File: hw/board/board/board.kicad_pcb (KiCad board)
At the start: 2 copper layers, 36 parts, among them J1 DB15_Female_HighDensity_Mount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, J2 10029449-111RLF, J3 SI-50170-F, J4 USB4085-GF-A_REVB, J5 USB_A_Stacked, J6 USB_A_Stacked, SW1 SW_DIP_x08, SW2 SW_Push, SW3 SW_Push, U18 MAX3421E, U19 TUSB2046BVFR, U20 FT4232H, U7 W65C02P

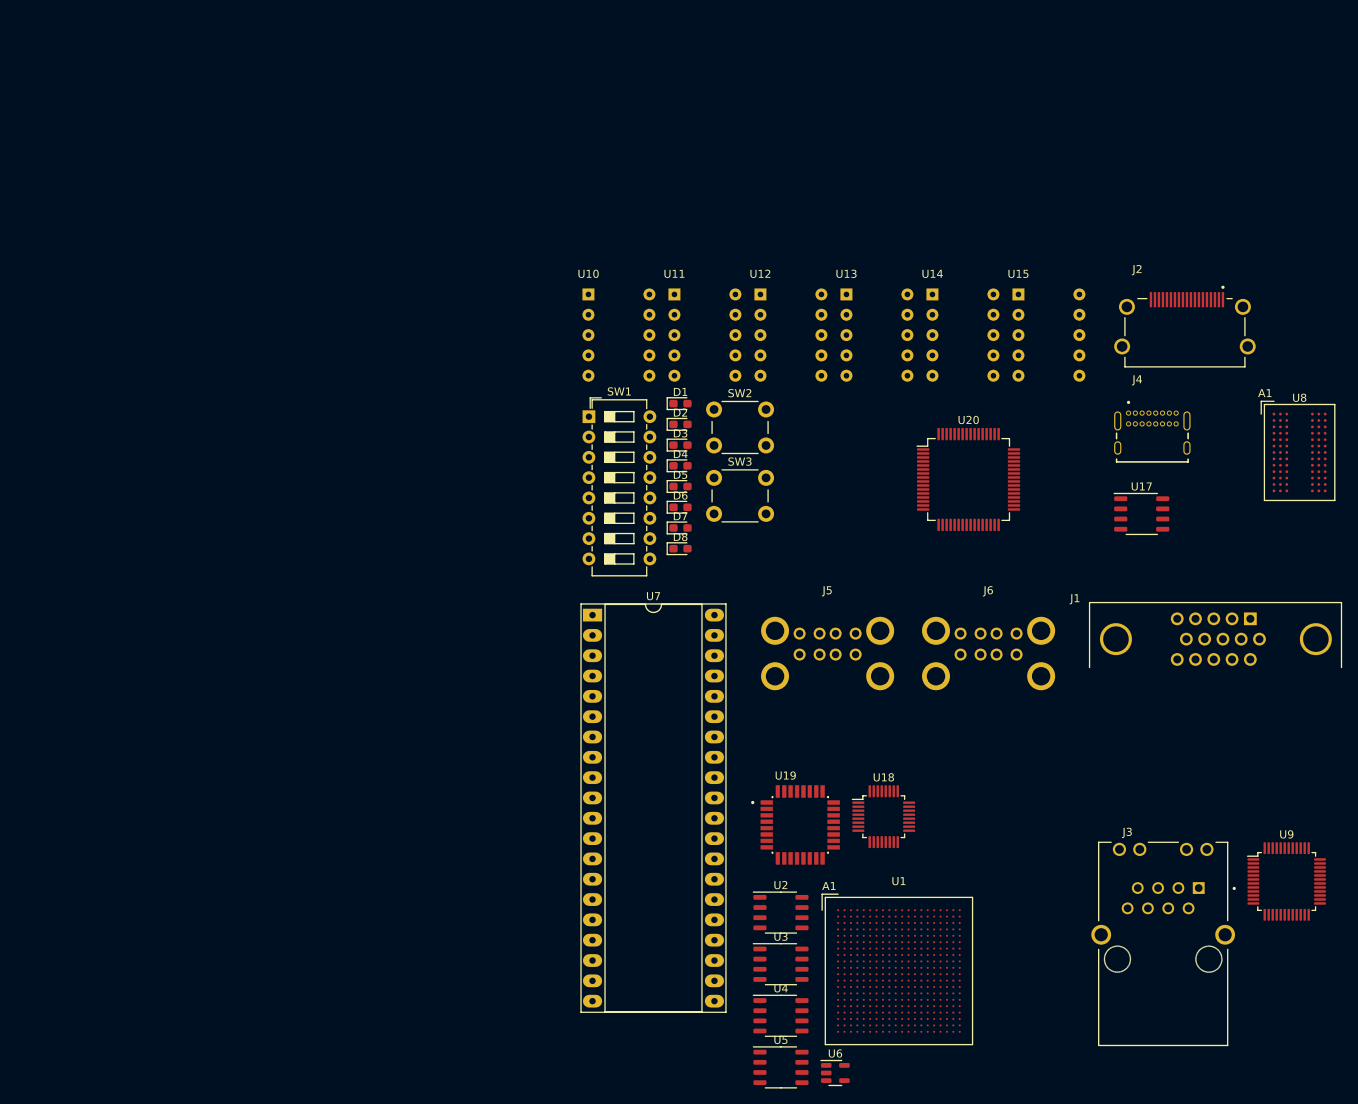
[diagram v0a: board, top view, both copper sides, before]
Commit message: Add wires to fpga block (but don't connect them)
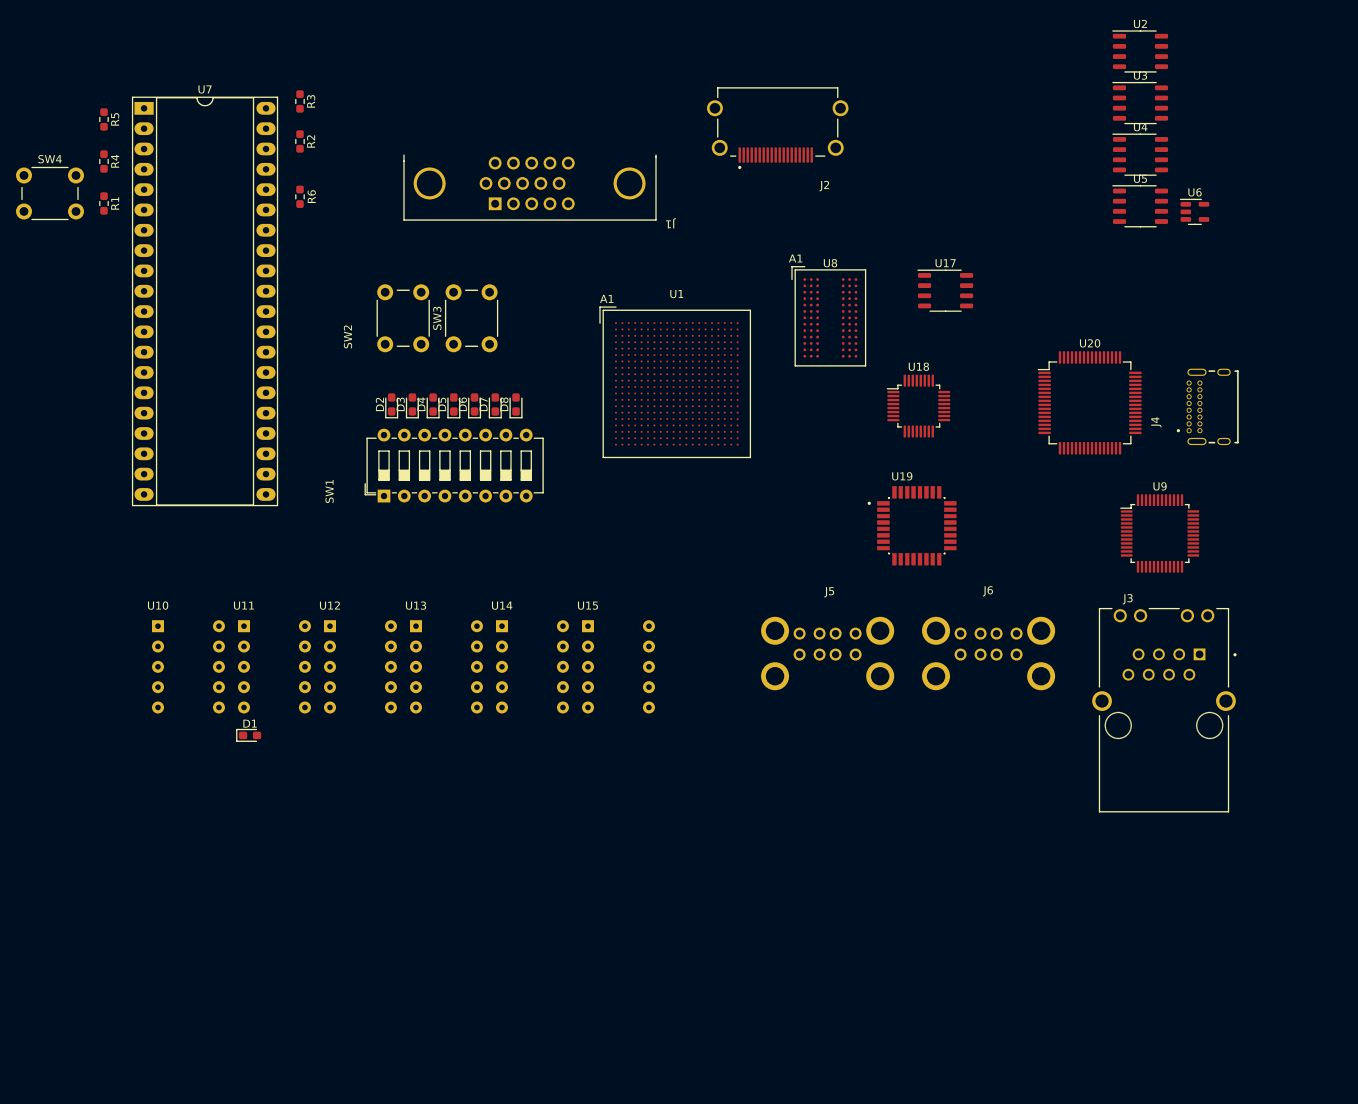
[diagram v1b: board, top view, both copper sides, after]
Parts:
- added R1: 10K, Resistor_SMD:R_0603_1608Metric_Pad0.98x0.95mm_HandSolder, F.Cu at (34.0, 37.5)
- added R2: 10K, Resistor_SMD:R_0603_1608Metric_Pad0.98x0.95mm_HandSolder, F.Cu at (58.5, 29.8)
- added R3: 10K, Resistor_SMD:R_0603_1608Metric_Pad0.98x0.95mm_HandSolder, F.Cu at (58.5, 24.8)
- added R4: 10K, Resistor_SMD:R_0603_1608Metric_Pad0.98x0.95mm_HandSolder, F.Cu at (34.0, 32.2)
- added R5: 10K, Resistor_SMD:R_0603_1608Metric_Pad0.98x0.95mm_HandSolder, F.Cu at (34.0, 27.0)
- added R6: 10K, Resistor_SMD:R_0603_1608Metric_Pad0.98x0.95mm_HandSolder, F.Cu at (58.5, 36.7)
- added SW4: SW_Push, Button_Switch_THT:SW_PUSH_6mm_H5mm, F.Cu at (24.0, 34.0)
- moved U5 116.6 mm to (163.6, 37.9)
- moved U2 116.6 mm to (163.6, 18.5)
- moved U3 116.6 mm to (163.6, 24.9)
- moved U6 116.6 mm to (170.4, 38.5)
- moved U4 116.6 mm to (163.6, 31.4)
- moved U7 84.6 mm to (39.0, 25.6)
- moved J1 83.3 mm to (99.7, 35.0), turned to 180 degrees
- moved U1 78.5 mm to (105.6, 60.0)
- moved U10 67.9 mm to (40.8, 90.3)
- moved U11 67.9 mm to (51.5, 90.3)
- moved U12 67.9 mm to (62.2, 90.3)
- moved U13 67.9 mm to (73.0, 90.3)
- moved U14 67.9 mm to (83.8, 90.3)
- moved U15 67.9 mm to (94.5, 90.3)
- moved D1 67.9 mm to (52.3, 104.0)
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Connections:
- U7 pad 1: unconnected-(U7-~{VPB}-Pad1) -> /cpu/~{CPU_VPB}
- U7 pad 10: unconnected-(U7-A1-Pad10) -> /cpu/CPU_ADDR1
- U7 pad 11: unconnected-(U7-A2-Pad11) -> /cpu/CPU_ADDR2
- U7 pad 12: unconnected-(U7-A3-Pad12) -> /cpu/CPU_ADDR3
- U7 pad 13: unconnected-(U7-A4-Pad13) -> /cpu/CPU_ADDR4
- U7 pad 14: unconnected-(U7-A5-Pad14) -> /cpu/CPU_ADDR5
- U7 pad 15: unconnected-(U7-A6-Pad15) -> /cpu/CPU_ADDR6
- U7 pad 16: unconnected-(U7-A7-Pad16) -> /cpu/CPU_ADDR7
- U7 pad 17: unconnected-(U7-A8-Pad17) -> /cpu/CPU_ADDR8
- U7 pad 18: unconnected-(U7-A9-Pad18) -> /cpu/CPU_ADDR9
- U7 pad 19: unconnected-(U7-A10-Pad19) -> /cpu/CPU_ADDR10
- U7 pad 2: unconnected-(U7-RDY-Pad2) -> /cpu/CPU_RDY
- U7 pad 20: unconnected-(U7-A11-Pad20) -> /cpu/CPU_ADDR11
- U7 pad 21: unconnected-(U7-VSS-Pad21) -> GND
- U7 pad 22: unconnected-(U7-A12-Pad22) -> /cpu/CPU_ADDR12
- U7 pad 23: unconnected-(U7-A13-Pad23) -> /cpu/CPU_ADDR13
- U7 pad 24: unconnected-(U7-A14-Pad24) -> /cpu/CPU_ADDR14
- U7 pad 25: unconnected-(U7-A15-Pad25) -> /cpu/CPU_ADDR15
- U7 pad 26: unconnected-(U7-D7-Pad26) -> /cpu/CPU_DATA7
- U7 pad 27: unconnected-(U7-D6-Pad27) -> /cpu/CPU_DATA6
- U7 pad 28: unconnected-(U7-D5-Pad28) -> /cpu/CPU_DATA5
- U7 pad 29: unconnected-(U7-D4-Pad29) -> /cpu/CPU_DATA4
- U7 pad 30: unconnected-(U7-D3-Pad30) -> /cpu/CPU_DATA3
- U7 pad 31: unconnected-(U7-D2-Pad31) -> /cpu/CPU_DATA2
- U7 pad 32: unconnected-(U7-D1-Pad32) -> /cpu/CPU_DATA1
- U7 pad 33: unconnected-(U7-D0-Pad33) -> /cpu/CPU_DATA0
- U7 pad 34: unconnected-(U7-~{RWB}-Pad34) -> /cpu/~{CPU_RWB}
- U7 pad 36: unconnected-(U7-BE-Pad36) -> /cpu/CPU_BE
- U7 pad 37: unconnected-(U7-PHI2-Pad37) -> /cpu/CPU_PHI2
- U7 pad 38: unconnected-(U7-~{SOB}-Pad38) -> Net-(U7-~{SOB})
- U7 pad 4: unconnected-(U7-~{IRQB}-Pad4) -> /cpu/~{CPU_IRQB}
- U7 pad 40: unconnected-(U7-~{RESB}-Pad40) -> /cpu/~{CPU_RESB}
- U7 pad 5: unconnected-(U7-~{MLB}-Pad5) -> /cpu/~{CPU_MLB}
- U7 pad 6: unconnected-(U7-~{NMIB}-Pad6) -> /cpu/~{CPU_NMIB}
- U7 pad 7: unconnected-(U7-SYNC-Pad7) -> /cpu/CPU_SYNC
- U7 pad 8: unconnected-(U7-VDD-Pad8) -> +3V3
- U7 pad 9: unconnected-(U7-A0-Pad9) -> /cpu/CPU_ADDR0

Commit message: Start work on ddr
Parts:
- added R10: 15R, Resistor_SMD:R_0402_1005Metric, F.Cu at (218.2, 77.5)
- added R11: 15R, Resistor_SMD:R_0402_1005Metric, F.Cu at (225.2, 77.5)
- added R12: 15R, Resistor_SMD:R_0402_1005Metric, F.Cu at (221.2, 77.5)
- added R13: 15R, Resistor_SMD:R_0402_1005Metric, F.Cu at (223.2, 77.5)
- added R14: 15R, Resistor_SMD:R_0402_1005Metric, F.Cu at (220.2, 77.5)
- added R15: 15R, Resistor_SMD:R_0402_1005Metric, F.Cu at (222.2, 77.5)
- added R17: 15R, Resistor_SMD:R_0402_1005Metric, F.Cu at (225.2, 44.6)
- added R18: 15R, Resistor_SMD:R_0402_1005Metric, F.Cu at (225.2, 47.1)
- added R19: 240R, Resistor_SMD:R_0402_1005Metric, F.Cu at (225.2, 49.6)
- added R20: 1k, Resistor_SMD:R_0402_1005Metric, F.Cu at (225.2, 52.1)
- added R21: 1k, Resistor_SMD:R_0402_1005Metric, F.Cu at (225.2, 54.6)
- added R22: 40R, Resistor_SMD:R_0402_1005Metric, F.Cu at (220.6, 94.3)
- added R23: 40R, Resistor_SMD:R_0402_1005Metric, F.Cu at (223.6, 94.3)
- added R24: 40R, Resistor_SMD:R_0402_1005Metric, F.Cu at (217.6, 94.3)
- added R25: 40R, Resistor_SMD:R_0402_1005Metric, F.Cu at (214.6, 88.0)
- added R26: 40R, Resistor_SMD:R_0402_1005Metric, F.Cu at (229.0, 89.0)
- added R27: 40R, Resistor_SMD:R_0402_1005Metric, F.Cu at (214.6, 89.0)
- added R28: 40R, Resistor_SMD:R_0402_1005Metric, F.Cu at (229.0, 90.0)
- added R29: 40R, Resistor_SMD:R_0402_1005Metric, F.Cu at (214.6, 90.0)
- added R30: 40R, Resistor_SMD:R_0402_1005Metric, F.Cu at (229.0, 91.0)
- added R31: 40R, Resistor_SMD:R_0402_1005Metric, F.Cu at (219.6, 94.3)
- added R32: 40R, Resistor_SMD:R_0402_1005Metric, F.Cu at (229.0, 87.0)
- added R33: 40R, Resistor_SMD:R_0402_1005Metric, F.Cu at (224.6, 94.3)
- added R34: 40R, Resistor_SMD:R_0402_1005Metric, F.Cu at (222.6, 94.3)
- added R35: 40R, Resistor_SMD:R_0402_1005Metric, F.Cu at (218.6, 94.3)
- added R36: 40R, Resistor_SMD:R_0402_1005Metric, F.Cu at (225.6, 94.3)
- added R37: 40R, Resistor_SMD:R_0402_1005Metric, F.Cu at (214.6, 87.0)
- added R38: 40R, Resistor_SMD:R_0402_1005Metric, F.Cu at (229.0, 88.0)
- added R39: 40R, Resistor_SMD:R_0402_1005Metric, F.Cu at (221.6, 94.3)
- added R40: 40R, Resistor_SMD:R_0402_1005Metric, F.Cu at (233.9, 52.1)
- added R41: 40R, Resistor_SMD:R_0402_1005Metric, F.Cu at (233.9, 54.6)
- added R42: 40R, Resistor_SMD:R_0402_1005Metric, F.Cu at (233.9, 57.1)
- added R43: 40R, Resistor_SMD:R_0402_1005Metric, F.Cu at (233.9, 59.7)
- added R44: 40R, Resistor_SMD:R_0402_1005Metric, F.Cu at (233.9, 62.2)
- added R45: 40R, Resistor_SMD:R_0402_1005Metric, F.Cu at (233.9, 64.7)
- added R46: 240R, Resistor_SMD:R_0402_1005Metric, F.Cu at (240.3, 44.6)
- added R7: 100R, Resistor_SMD:R_0402_1005Metric, F.Cu at (220.9, 44.6)
- added R8: 15R, Resistor_SMD:R_0402_1005Metric, F.Cu at (219.2, 77.5)
- added R9: 15R, Resistor_SMD:R_0402_1005Metric, F.Cu at (224.2, 77.5)
- moved U1 152.7 mm to (256.2, 85.2)
- moved U8 102.7 mm to (221.8, 85.4)
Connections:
- U1 pad K1: unconnected-(U1K-DDR_BA2-PadK1) -> /ddr/DDR_BA2
- U1 pad K2: unconnected-(U1K-DDR_BA2-PadK2) -> /ddr/DDR_BA1
- U1 pad K3: unconnected-(U1K-DDR_BA0-PadK3) -> /ddr/DDR_BA0
- U1 pad K4: unconnected-(U1K-DDR_WE_N-PadK4) -> /ddr/DDR_WE#
- U1 pad L4: unconnected-(U1K-DDR_RST_N-PadL4) -> /ddr/DDR_RESET#
- U1 pad L6: unconnected-(U1K-DDR_ODT-PadL6) -> /ddr/DDR_ODT
- U1 pad L7: unconnected-(U1K-VCCIO_DDR-PadL7) -> +1V35
- U1 pad M4: unconnected-(U1K-DDR_RAS_N-PadM4) -> /ddr/DDR_RAS#
- U1 pad M6: unconnected-(U1K-DDR_A13-PadM6) -> /ddr/DDR_A13
- U1 pad N4: unconnected-(U1K-DDR_A14-PadN4) -> /ddr/DDR_A14
- U1 pad N5: unconnected-(U1K-DDR_A11-PadN5) -> /ddr/DDR_A11
- U1 pad N6: unconnected-(U1K-DDR_CKE-PadN6) -> /ddr/DDR_CKE
- U1 pad N7: unconnected-(U1K-VCCIO_DDR-PadN7) -> +1V35
- U1 pad P4: unconnected-(U1K-DDR_A12-PadP4) -> /ddr/DDR_A12
- U1 pad P5: unconnected-(U1K-VCCIO_DDR-PadP5) -> +1V35
- U1 pad P6: unconnected-(U1K-DDR_CAS_N-PadP6) -> /ddr/DDR_CAS#
- U1 pad R1: unconnected-(U1K-DDR_A8-PadR1) -> /ddr/DDR_A8
- U1 pad R2: unconnected-(U1K-VCCIO_DDR-PadR2) -> +1V35
- U1 pad R3: unconnected-(U1K-DDR_CK-PadR3) -> /ddr/DDR_CK
- U1 pad R4: unconnected-(U1K-DDR_CK_N-PadR4) -> /ddr/DDR_CK#
- U1 pad R5: unconnected-(U1K-DDR_A10-PadR5) -> /ddr/DDR_A10
- U1 pad R6: unconnected-(U1K-DDR_CS_N-PadR6) -> /ddr/DDR_CS#
- U1 pad R7: unconnected-(U1K-VCCIO_DDR-PadR7) -> +1V35
- U1 pad T1: unconnected-(U1K-DDR_A7-PadT1) -> /ddr/DDR_A7
- U1 pad T2: unconnected-(U1K-DDR_A9-PadT2) -> /ddr/DDR_A9
- U1 pad T3: unconnected-(U1K-DDR_A4-PadT3) -> /ddr/DDR_A4
- U1 pad T4: unconnected-(U1K-DDR_A6-PadT4) -> /ddr/DDR_A6
- U1 pad T5: unconnected-(U1K-DDR_A5-PadT5) -> /ddr/DDR_A5
- U1 pad T6: unconnected-(U1K-DDR_A3-PadT6) -> /ddr/DDR_A3
- U1 pad U1: unconnected-(U1K-DDR_DQS_N0-PadU1) -> /ddr/DDR_DQS#
- U1 pad U2: unconnected-(U1K-DDR_DQ3-PadU2) -> /ddr/DDR_DQ3
- U1 pad U3: unconnected-(U1K-DDR_DQ0-PadU3) -> /ddr/DDR_DQ0
- U1 pad U4: unconnected-(U1K-DDR_A0-PadU4) -> /ddr/DDR_A0
- U1 pad V1: unconnected-(U1K-DDR_DQS0-PadV1) -> /ddr/DDR_DQS
- U1 pad V3: unconnected-(U1K-DDR_DQ2-PadV3) -> /ddr/DDR_DQ2
- U1 pad V4: unconnected-(U1K-DDR_VREF-PadV4) -> /fpga/VTT
- U1 pad V5: unconnected-(U1K-DDR_A2-PadV5) -> /ddr/DDR_A2
- U1 pad W1: unconnected-(U1K-DDR_DM0-PadW1) -> /ddr/DDR_DM
- U1 pad W2: unconnected-(U1K-DDR_DQ4-PadW2) -> /ddr/DDR_DQ4
- U1 pad W3: unconnected-(U1K-DDR_DQ1-PadW3) -> /ddr/DDR_DQ1
- U1 pad W4: unconnected-(U1K-VCCIO_DDR-PadW4) -> +1V35
- U1 pad W5: unconnected-(U1K-DDR_A1-PadW5) -> /ddr/DDR_A1
- U1 pad Y2: unconnected-(U1K-DDR_DQ7-PadY2) -> /ddr/DDR_DQ7
- U1 pad Y3: unconnected-(U1K-DDR_DQ5-PadY3) -> /ddr/DDR_DQ5
- U1 pad Y4: unconnected-(U1K-DDR_DQ6-PadY4) -> /ddr/DDR_DQ6
- U1 pad Y5: unconnected-(U1K-DDR_ZQ-PadY5) -> Net-(U1K-DDR_ZQ)
- U8 pad A1: unconnected-(U8A-VSS-PadA1) -> GND
- U8 pad A2: unconnected-(U8A-VDD-PadA2) -> +1V35
- U8 pad A8: unconnected-(U8A-VSS-PadA8) -> GND
- U8 pad A9: unconnected-(U8A-VDD-PadA9) -> +1V35
- U8 pad B1: unconnected-(U8A-VSS-PadB1) -> GND
- U8 pad B2: unconnected-(U8A-VSSQ-PadB2) -> GND
- U8 pad B3: unconnected-(U8B-DQ0-PadB3) -> Net-(U8B-DQ0)
- U8 pad B7: unconnected-(U8B-DM/TDQS-PadB7) -> Net-(U8B-DM/TDQS)
- U8 pad B8: unconnected-(U8A-VSSQ-PadB8) -> GND
- U8 pad B9: unconnected-(U8A-VDDQ-PadB9) -> +1V35
- U8 pad C1: unconnected-(U8A-VDDQ-PadC1) -> +1V35
- U8 pad C2: unconnected-(U8B-DQ2-PadC2) -> Net-(U8B-DQ2)
- U8 pad C3: unconnected-(U8B-DQS-PadC3) -> Net-(U8B-DQS)
- U8 pad C7: unconnected-(U8B-DQ1-PadC7) -> Net-(U8B-DQ1)
- U8 pad C8: unconnected-(U8B-DQ3-PadC8) -> Net-(U8B-DQ3)
- U8 pad C9: unconnected-(U8A-VSSQ-PadC9) -> GND
- U8 pad D1: unconnected-(U8A-VSSQ-PadD1) -> GND
- U8 pad D2: unconnected-(U8B-DQ6-PadD2) -> Net-(U8B-DQ6)
- U8 pad D3: unconnected-(U8B-DQS#-PadD3) -> Net-(U8B-DQS#)
- U8 pad D7: unconnected-(U8A-VDD-PadD7) -> +1V35
- U8 pad D8: unconnected-(U8A-VSS-PadD8) -> GND
- U8 pad D9: unconnected-(U8A-VSSQ-PadD9) -> GND
- U8 pad E1: unconnected-(U8A-VREFDQ-PadE1) -> /ddr/VTT
- U8 pad E2: unconnected-(U8A-VDDQ-PadE2) -> +1V35
- U8 pad E3: unconnected-(U8B-DQ4-PadE3) -> Net-(U8B-DQ4)
- U8 pad E7: unconnected-(U8B-DQ7-PadE7) -> Net-(U8B-DQ7)
- U8 pad E8: unconnected-(U8B-DQ5-PadE8) -> Net-(U8B-DQ5)
- U8 pad E9: unconnected-(U8A-VDDQ-PadE9) -> +1V35
- U8 pad F2: unconnected-(U8A-VSS-PadF2) -> GND
- U8 pad F3: unconnected-(U8B-RAS#-PadF3) -> /ddr/DDR_RAS#
- U8 pad F7: unconnected-(U8B-CK-PadF7) -> /ddr/DDR_CK
- U8 pad F8: unconnected-(U8A-VSS-PadF8) -> GND
- U8 pad G1: unconnected-(U8B-ODT-PadG1) -> /ddr/DDR_ODT
- U8 pad G2: unconnected-(U8A-VDD-PadG2) -> +1V35
- U8 pad G3: unconnected-(U8B-CAS#-PadG3) -> /ddr/DDR_CAS#
- U8 pad G7: unconnected-(U8B-CK#-PadG7) -> /ddr/DDR_CK#
- U8 pad G8: unconnected-(U8A-VDD-PadG8) -> +1V35
- U8 pad G9: unconnected-(U8B-CKE-PadG9) -> /ddr/DDR_CKE
- U8 pad H2: unconnected-(U8B-CS#-PadH2) -> /ddr/DDR_CS#
- U8 pad H3: unconnected-(U8B-WE#-PadH3) -> /ddr/DDR_WE#
- U8 pad H7: unconnected-(U8B-A10/AP-PadH7) -> /ddr/DDR_A10
- U8 pad H8: unconnected-(U8B-ZQ-PadH8) -> Net-(U8B-ZQ)
- U8 pad J1: unconnected-(U8A-VSS-PadJ1) -> GND
- U8 pad J2: unconnected-(U8B-BA0-PadJ2) -> /ddr/DDR_BA0
- U8 pad J3: unconnected-(U8B-BA2-PadJ3) -> /ddr/DDR_BA2
- U8 pad J8: unconnected-(U8A-VREFCA-PadJ8) -> /ddr/VTT
- U8 pad J9: unconnected-(U8A-VSS-PadJ9) -> GND
- U8 pad K1: unconnected-(U8A-VDD-PadK1) -> +1V35
- U8 pad K2: unconnected-(U8B-A3-PadK2) -> /ddr/DDR_A3
- U8 pad K3: unconnected-(U8B-A0-PadK3) -> /ddr/DDR_A0
- U8 pad K7: unconnected-(U8B-A12/BC#-PadK7) -> /ddr/DDR_A12
- U8 pad K8: unconnected-(U8B-BA1-PadK8) -> /ddr/DDR_BA1
- U8 pad K9: unconnected-(U8A-VDD-PadK9) -> +1V35
- U8 pad L1: unconnected-(U8A-VSS-PadL1) -> GND
- U8 pad L2: unconnected-(U8B-A5-PadL2) -> /ddr/DDR_A5
- U8 pad L3: unconnected-(U8B-A2-PadL3) -> /ddr/DDR_A2
- U8 pad L7: unconnected-(U8B-A1-PadL7) -> /ddr/DDR_A1
- U8 pad L8: unconnected-(U8B-A4-PadL8) -> /ddr/DDR_A4
- U8 pad L9: unconnected-(U8A-VSS-PadL9) -> GND
- U8 pad M1: unconnected-(U8A-VDD-PadM1) -> +1V35
- U8 pad M2: unconnected-(U8B-A7-PadM2) -> /ddr/DDR_A7
- U8 pad M3: unconnected-(U8B-A9-PadM3) -> /ddr/DDR_A9
- U8 pad M7: unconnected-(U8B-A11-PadM7) -> /ddr/DDR_A11
- U8 pad M8: unconnected-(U8B-A6-PadM8) -> /ddr/DDR_A6
- U8 pad M9: unconnected-(U8A-VDD-PadM9) -> +1V35
- U8 pad N1: unconnected-(U8A-VSS-PadN1) -> GND
- U8 pad N2: unconnected-(U8B-RESET#-PadN2) -> /ddr/DDR_RESET#
- U8 pad N3: unconnected-(U8B-A13-PadN3) -> /ddr/DDR_A13
- U8 pad N7: unconnected-(U8B-A14-PadN7) -> /ddr/DDR_A14
- U8 pad N8: unconnected-(U8B-A8-PadN8) -> /ddr/DDR_A8
- U8 pad N9: unconnected-(U8A-VSS-PadN9) -> GND
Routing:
- net GND: track 0.00 -> 12.2 mm, vias 0 -> 15
- net +1V35: track 0.00 -> 9.13 mm, vias 0 -> 13
- net /ddr/DDR_BA2: track 0.00 -> 7.61 mm, vias 0 -> 1
- net Net-(U8B-DQ5): track 0.00 -> 7.23 mm
- net /ddr/DDR_A2: track 0.00 -> 6.82 mm, vias 0 -> 1
- net /ddr/DDR_A0: track 0.00 -> 6.81 mm, vias 0 -> 1
- net Net-(U8B-DQ7): track 0.00 -> 6.70 mm
- net /ddr/DDR_A12: track 0.00 -> 6.64 mm, vias 0 -> 1
- net Net-(U8B-DQ6): track 0.00 -> 6.59 mm
- net Net-(U8B-DQ4): track 0.00 -> 6.55 mm
- net /ddr/DDR_A1: track 0.00 -> 5.91 mm, vias 0 -> 1
- net /ddr/DDR_A10: track 0.00 -> 5.42 mm
- net /ddr/DDR_A6: track 0.00 -> 5.34 mm, vias 0 -> 1
- net /ddr/DDR_A9: track 0.00 -> 5.28 mm, vias 0 -> 1
- net /ddr/DDR_A11: track 0.00 -> 5.21 mm, vias 0 -> 1
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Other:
- copper layers 2 -> 6
- board text added: "R22-39"
- board text added: "R8-15"
